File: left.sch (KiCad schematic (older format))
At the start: 63 parts, among them J1 Speaker, J2 reset, J3 ISP, J7 Sig, J9 UTC16-G, P3 WS2812, P4 SJ-43514-SMT, SW1 Socket, SW10 Socket, SW11 Socket, SW12 Socket, SW13 Socket, SW14 Socket, SW15 Socket, SW16 Socket, SW17 Socket, SW18 Socket, SW19 Socket, SW2 Socket, SW20 Socket, SW21 Socket, SW22 Socket, SW23 Socket, SW24 Socket, SW3 Socket, SW4 Socket, SW49 FSMSM, SW5 Socket, SW6 Socket, SW7 Socket, SW8 Socket, SW9 Socket, U1 ATMega32U4, Y1 16MHz

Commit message: Added WS2812B leds to one half
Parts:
- added C10, C11, C12, C13, C14, C9: 1uF, Capacitor_SMD:C_0603_1608Metric, symbol vitamins_included-rescue:C_Small-RESCUE-lets_split_panel-lets_split_panel-rescue
- added D29, D30, D31, D32, D33, D34: WS2812B, LED_SMD:LED_WS2812B_PLCC4_5.0x5.0mm_P3.2mm, symbol LED:WS2812B
- J9: symbol Connector:USB_C_Receptacle -> vitamins_included-rescue:USB_C_Receptacle-Connector
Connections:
- wire segments 220 -> 277

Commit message: Fixed rotated LEDs, added config jumpers
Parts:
- removed J7: Sig, Pin_Headers:Pin_Header_Straight_1x01_Pitch2.54mm, symbol vitamins_included-rescue:Conn_01x01-RESCUE-lets_split_panel-lets_split_panel-re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
- removed J9: UTC16-G, Connector_USB:USB_C_Receptacle_Palconn_UTC16-G, symbol vitamins_included-rescue:USB_C_Receptacle-Connector
- removed P4: SJ-43514-SMT, Connectors:SJ-4351X-SMT, symbol vitamins_included-rescue:Conn_01x04-RESCUE-lets_split_panel-lets_split_panel-re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
- added J9: UTC16-G, Connector_USB:USB_C_Receptacle_Palconn_UTC16-G, symbol Connector:USB_C_Receptacle_USB2.0
- added JP4: WS_MODE, Jumper:SolderJumper-3_P1.3mm_Bridged12_RoundedPad1.0x1.5mm, symbol Jumper:SolderJumper_3_Bridged12
- added JP5: WS_OUT, Jumper:SolderJumper-3_P1.3mm_Bridged12_RoundedPad1.0x1.5mm, symbol Jumper:SolderJumper_3_Bridged12
- added P4: SJ-43514-SMT, UJ31-CH-31-SMT-TR:SJ-4351X-SMT, symbol Connector:AudioJack4
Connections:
- net labels added: WS2812-in, WS2812-out
- net labels removed: wd2812-in
- wire segments 277 -> 272
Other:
- moved on the sheet: C10, C11, C12, C13, C14, C9, D29, D30, D31, D32, D33, D34

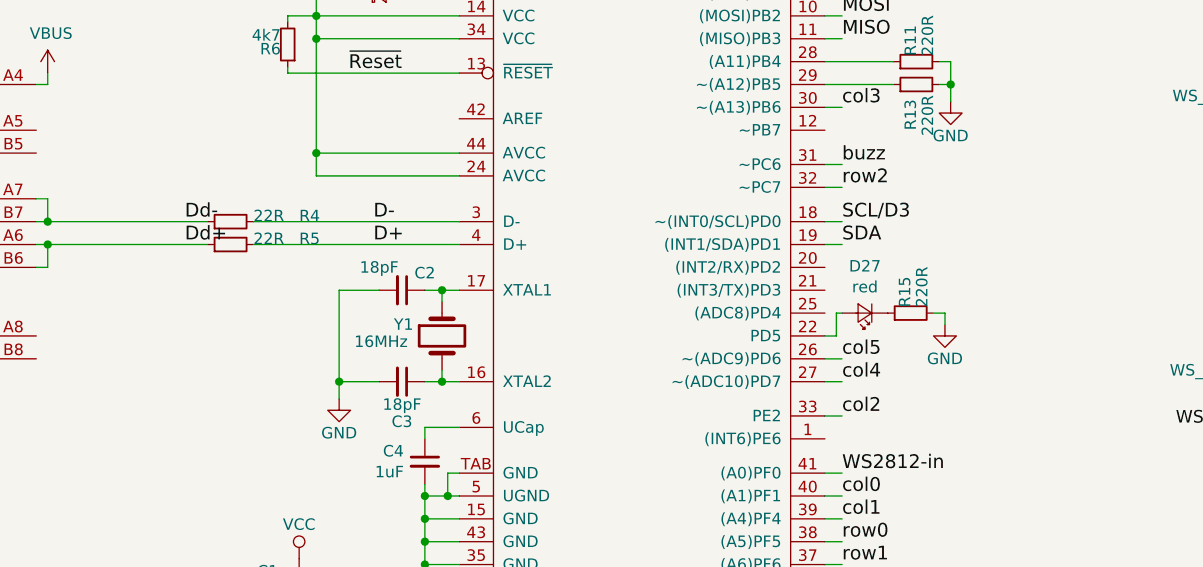
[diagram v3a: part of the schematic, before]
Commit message: Added MPN to DFU LED
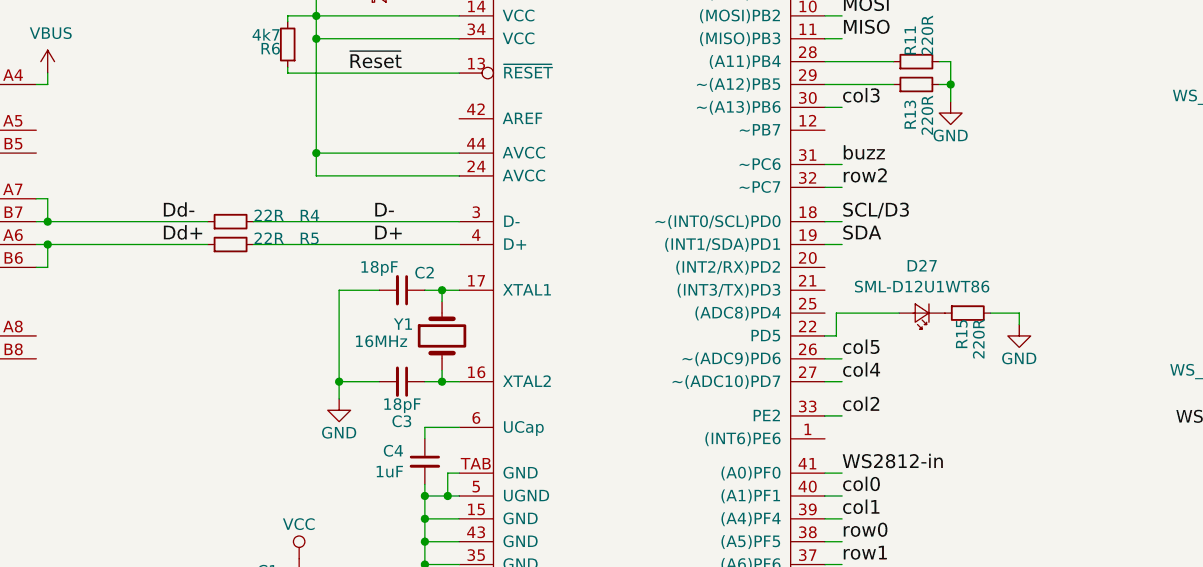
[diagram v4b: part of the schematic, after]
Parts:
- D27: value red -> SML-D12U1WT86
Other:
- moved on the sheet: D27, R15
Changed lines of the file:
@@
 Text Label 4425 1150 0    60   ~ 0
 SCL/D3
-Text Label 2375 5100 0    60   ~ 0
+Text Label 2275 5100 0    60   ~ 0
 Dd-
-Text Label 2375 5200 0    60   ~ 0
+Text Label 2275 5200 0    60   ~ 0
 Dd+
 $Comp
@@
 L Device:LED_Small D27
 U 1 1 5B5D7908
-P 5350 5500
-F 0 "D27" H 5350 5295 50  0000 C CNN
-F 1 "red" H 5350 5386 50  0000 C CNN
-F 2 "LED_SMD:LED_0603_1608Metric_Castellated" V 5350 5500 50  0001 C CNN
-F 3 "~" V 5350 5500 50  0001 C CNN
-	1    5350 5500
+P 5600 5500
+F 0 "D27" H 5600 5295 50  0000 C CNN
+F 1 "SML-D12U1WT86" H 5600 5386 50  0000 C CNN
+F 2 "LED_SMD:LED_0603_1608Metric_Castellated" V 5600 5500 50  0001 C CNN
+F 3 "~" V 5600 5500 50  0001 C CNN
+	1    5600 5500
 	-1   0    0    1
 $EndComp
@@
 	5225 5600 5225 5500
 Wire Wire Line
-	5225 5500 5250 5500
+	5225 5500 5500 5500
 $Comp
 L vitamins_included-rescue:R_Small-RESCUE-lets_split_panel-lets_split_panel-rescue R15
 U 1 1 5B5E58FB
-P 5550 5500
-F 0 "R15" H 5575 5525 50  0000 L CNN
-F 1 "220R" H 5575 5450 50  0000 L CNN
-F 2 "Resistor_SMD:R_0603_1608Metric" H 5550 5500 50  0001 C CNN
-F 3 "" H 5550 5500 50  0000 C CNN
-	1    5550 5500
-	0    -1   -1   0
-$EndComp
-Wire Wire Line
-	5650 5500 5700 5500
-Wire Wire Line
-	5700 5500 5700 5550
+P 5800 5500
+F 0 "R15" H 5825 5525 50  0000 L CNN
+F 1 "220R" H 5825 5450 50  0000 L CNN
+F 2 "Resistor_SMD:R_0603_1608Metric" H 5800 5500 50  0001 C CNN
+F 3 "" H 5800 5500 50  0000 C CNN
+	1    5800 5500
+	0    -1   1    0
+$EndComp
+Wire Wire Line
+	5900 5500 6025 5500
+Wire Wire Line
+	6025 5500 6025 5550
 $Comp
 L vitamins_included-rescue:GND-RESCUE-lets_split_panel-lets_split_panel-rescue #PWR0101
 U 1 1 5B621855
-P 5700 5550
-F 0 "#PWR0101" H 5700 5300 50  0001 C CNN
-F 1 "GND" H 5700 5400 50  0000 C CNN
-F 2 "" H 5700 5550 50  0000 C CNN
-F 3 "" H 5700 5550 50  0000 C CNN
-	1    5700 5550
-	1    0    0    -1
-$EndComp
+P 6025 5550
+F 0 "#PWR0101" H 6025 5300 50  0001 C CNN
+F 1 "GND" H 6025 5400 50  0000 C CNN
+F 2 "" H 6025 5550 50  0000 C CNN
+F 3 "" H 6025 5550 50  0000 C CNN
+	1    6025 5550
+	1    0    0    -1
+$EndComp

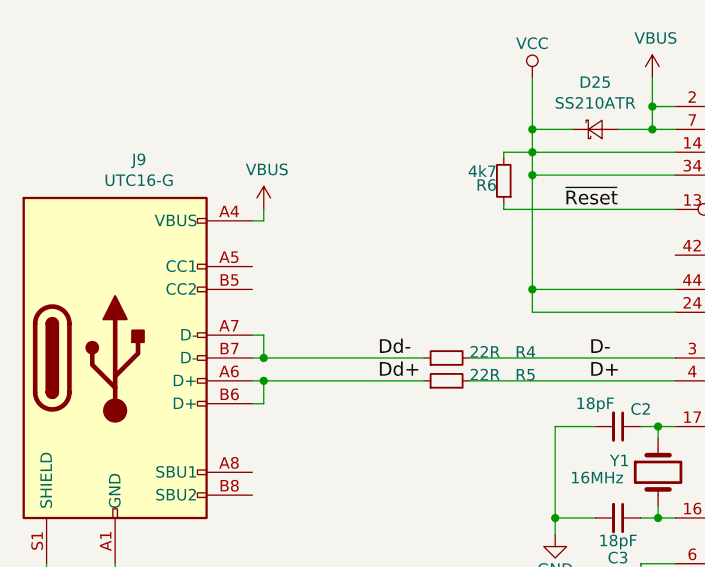
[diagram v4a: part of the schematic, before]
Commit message: Added 5k1 CC resistors
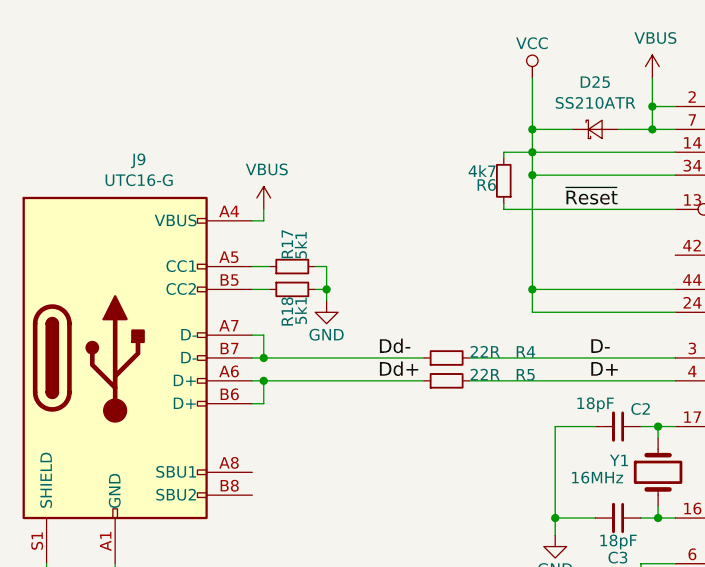
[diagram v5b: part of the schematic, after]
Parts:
- added R17, R18: 5k1, Resistor_SMD:R_0603_1608Metric, symbol vitamins_included-rescue:R_Small-RESCUE-lets_split_panel-lets_split_panel-rescue
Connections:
- net GND: now also R17.2, R18.2
- net at J9.A5 (CC1): now also R17.1
- net at J9.B5 (CC2): now also R18.1
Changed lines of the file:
@@
 Wire Wire Line
 	5250 6200 5175 6200
+$Comp
+L vitamins_included-rescue:R_Small-RESCUE-lets_split_panel-lets_split_panel-rescue R18
+U 1 1 5D1F5D3C
+P 1900 4800
+F 0 "R18" H 1930 4820 50  0000 L CNN
+F 1 "5k1" H 1930 4760 50  0000 L CNN
+F 2 "Resistor_SMD:R_0603_1608Metric" H 1900 4800 50  0001 C CNN
+F 3 "" H 1900 4800 50  0000 C CNN
+	1    1900 4800
+	0    -1   1    0
+$EndComp
+$Comp
+L vitamins_included-rescue:R_Small-RESCUE-lets_split_panel-lets_split_panel-rescue R17
+U 1 1 5D1F5FF4
+P 1900 4700
+F 0 "R17" H 1930 4720 50  0000 L CNN
+F 1 "5k1" H 1930 4660 50  0000 L CNN
+F 2 "Resistor_SMD:R_0603_1608Metric" H 1900 4700 50  0001 C CNN
+F 3 "" H 1900 4700 50  0000 C CNN
+	1    1900 4700
+	0    -1   -1   0
+$EndComp
+Wire Wire Line
+	1725 4800 1800 4800
+Wire Wire Line
+	1725 4700 1800 4700
+$Comp
+L vitamins_included-rescue:GND-RESCUE-lets_split_panel-lets_split_panel-rescue #PWR0111
+U 1 1 5D209478
+P 2050 4850
+F 0 "#PWR0111" H 2050 4600 50  0001 C CNN
+F 1 "GND" H 2050 4700 50  0000 C CNN
+F 2 "" H 2050 4850 50  0000 C CNN
+F 3 "" H 2050 4850 50  0000 C CNN
+	1    2050 4850
+	1    0    0    -1
+$EndComp
+Wire Wire Line
+	2050 4850 2050 4800
+Wire Wire Line
+	2050 4800 2000 4800
+Wire Wire Line
+	2000 4700 2050 4700
+Wire Wire Line
+	2050 4700 2050 4800
+Connection ~ 2050 4800
 $EndSCHEMATC

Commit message: Pre-cleanup
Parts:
- removed J1: Speaker, Buzzers_Beepers:Buzzer_12x9.5RM7.6, symbol vitamins_included-rescue:Conn_01x02-RESCUE-lets_split_panel-lets_split_panel-re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
- added J1: Buzzer, Buzzers_Beepers:Buzzer_12x9.5RM7.6, symbol Device:Buzzer
- added J11, J12, J13, J14, J15, J16, J17, J7: Conn_01x01, TestPoint:TestPoint_Pad_D1.5mm, symbol Connector_Generic:Conn_01x01
- R1, R2, R6: value 4k7 -> 4K7
- R17, R18: value 5k1 -> 5K1
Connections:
- net GND: now also J1.2 (+), J16.1 (Pin_1)
- net VCC: now also J17.1 (Pin_1)
- net at R3.2: now also J1.1 (-)
- net PE6: now reaches U1.1 ((INT6)PE6)
- net PE6: now also J13.1 (Pin_1)
- net PB7: now reaches U1.12 (~~PB7)
- net PB7: now also J14.1 (Pin_1)
- net PD2: now reaches U1.20 ((INT2/RX)PD2)
- net PD2: now also J12.1 (Pin_1)
- net PD3: now reaches U1.21 ((INT3/TX)PD3)
- net PD3: now also J7.1 (Pin_1)
- net PD4: now reaches U1.25 ((ADC8)PD4)
- net PD4: now also J11.1 (Pin_1)
- net PB0: now reaches U1.8 ((CS)PB0)
- net PB0: now also J15.1 (Pin_1)
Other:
- note added: "Connectivity"
- note added: "MCU"
- note added: "Matrix"
- note added: "WS2812B RGB\nUnderglow"
- moved on the sheet: C1, C10, C11, C12, C13, C14, C2, C3, C4, C9, D1, D10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

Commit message: Fixed symbols to not rely on rescue
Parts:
- C1, C10, C11, C12, C13, C14, C2, C3, C4, C9: symbol vitamins_included-rescue:C_Small-RESCUE-lets_split_panel-lets_split_panel-rescue -> Device:C_Small
- J3: symbol vitamins_included-rescue:Conn_02x03_Odd_Even-RESCUE-lets_split_panel-lets_split_panel-rescue -> Connector_Generic:Conn_02x03_Odd_Even
- JP1, JP2: symbol vitamins_included-rescue:Jumper-RESCUE-lets_split_panel-lets_split_panel-rescue -> Device:Jumper
- P3: symbol vitamins_included-rescue:Conn_01x03-RESCUE-lets_split_panel-lets_split_panel-rescue -> Connector_Generic:Conn_01x03
- R1, R11, R13, R15, R17, R18, R2, R3, R4, R5, R6: symbol vitamins_included-rescue:R_Small-RESCUE-lets_split_panel-lets_split_panel-rescue -> Device:R_Small
- SW1, SW10, SW11, SW12, SW13, SW14, SW15, SW16, SW17, SW18, SW19, SW2, SW20, SW21, SW22, SW23, SW24, SW3, SW4, SW5, SW6, SW7, SW8, SW9: symbol vitamins_included-rescue:SW_Push-RESCUE-lets_split_panel-lets_split_panel-rescue -> Switch:SW_Push
- U1: symbol vitamins_included-rescue:ATMega32U4-RESCUE-lets_split_panel-lets_split_panel-rescue -> 8Bit-MCU:ATMega32U4
- Y1: symbol vitamins_included-rescue:Crystal-RESCUE-lets_split_panel-lets_split_panel-rescue -> Device:Crystal

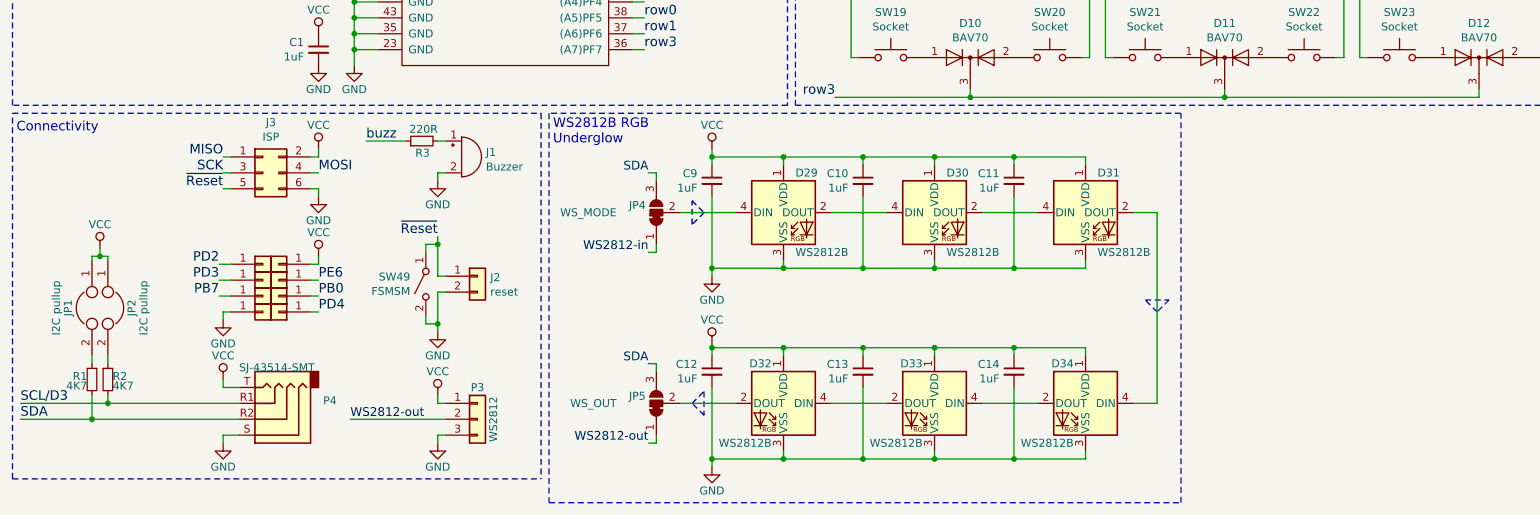
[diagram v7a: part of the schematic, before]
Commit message: Added footprint for AST1109MLTRQ buzzer
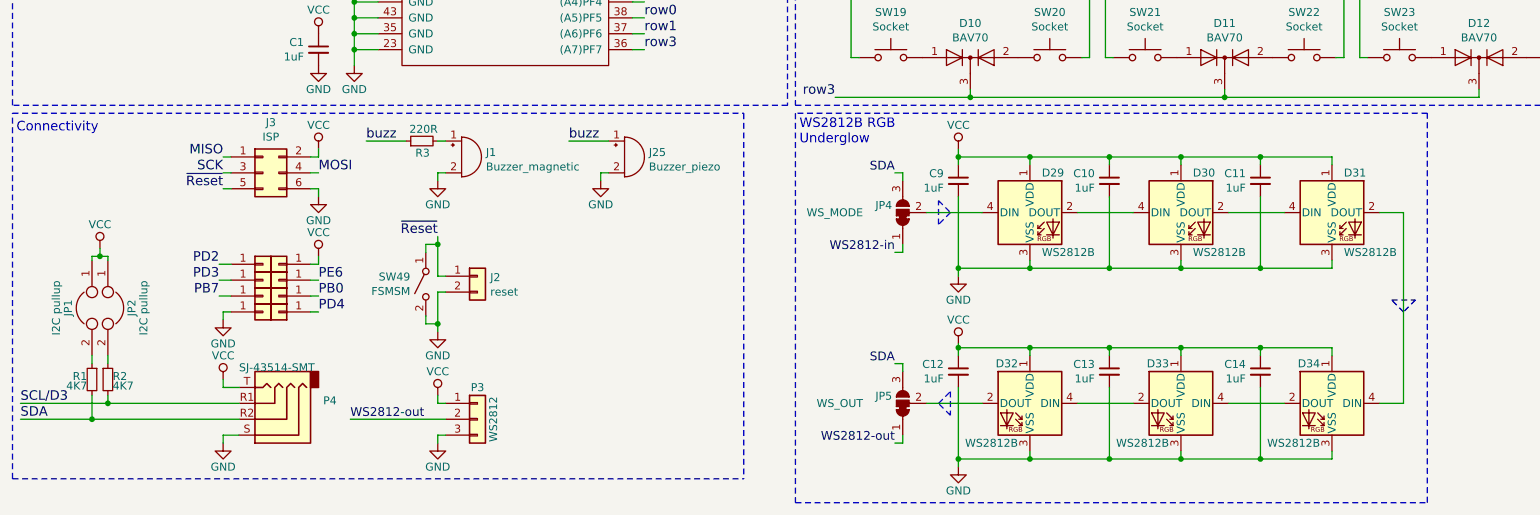
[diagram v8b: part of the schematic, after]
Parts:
- added J25: Buzzer_piezo, Buzzer_Beeper:Buzzer_Mallory_AST1109MLTRQ, symbol Device:Buzzer
- J1: value Buzzer -> Buzzer_magnetic
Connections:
- net GND: now also J25.2 (+)
- net buzz: now also J25.1 (-)
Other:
- moved on the sheet: C10, C11, C12, C13, C14, C9, D29, D30, D31, D32, D33, D34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
